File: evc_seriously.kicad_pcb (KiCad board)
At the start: 2 copper layers, 58 parts, among them J1 Screw_Terminal_01x10, J2 Conn_ARM_JTAG_SWD_10, J3 J_IN, J4 J_OUT, SW1 SW_Push, U1 TCA9517, U2 MPM3510A, U3 MPM3510A, U4 STM32F303K8Tx, U5 MIC2981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

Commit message: More routing of the board
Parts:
- C1, C2: footprint Capacitor_SMD:CP_Elec_5x5.8 -> Capacitor_SMD:C_0805_2012Metric
- moved JP1 94.0 mm to (190.2, 111.5)
- moved C11 91.7 mm to (166.1, 102.9), turned to 180 degrees
- moved U6 90.7 mm to (189.2, 116.8), turned to 90 degrees
- moved C13 86.1 mm to (185.4, 119.1), turned to 90 degrees
- moved JP2 85.2 mm to (186.4, 111.5)
- moved C10 83.2 mm to (166.1, 119.6)
- moved C9 80.4 mm to (155.0, 102.9)
- moved R10 67.9 mm to (90.9, 166.3), turned to 270 degrees
- moved C5 62.6 mm to (185.4, 114.6), turned to 90 degrees
- moved R11 57.1 mm to (90.9, 163.1), turned to 270 degrees
- moved C7 56.2 mm to (155.2, 110.5), turned to 180 degrees
- moved R3 56.2 mm to (91.7, 149.6), turned to 180 degrees
- moved U1 54.0 mm to (160.6, 104.8)
- moved C1 49.6 mm to (95.6, 160.5), turned to 180 degrees
- moved C3 48.7 mm to (168.9, 110.5), turned to 90 degrees
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
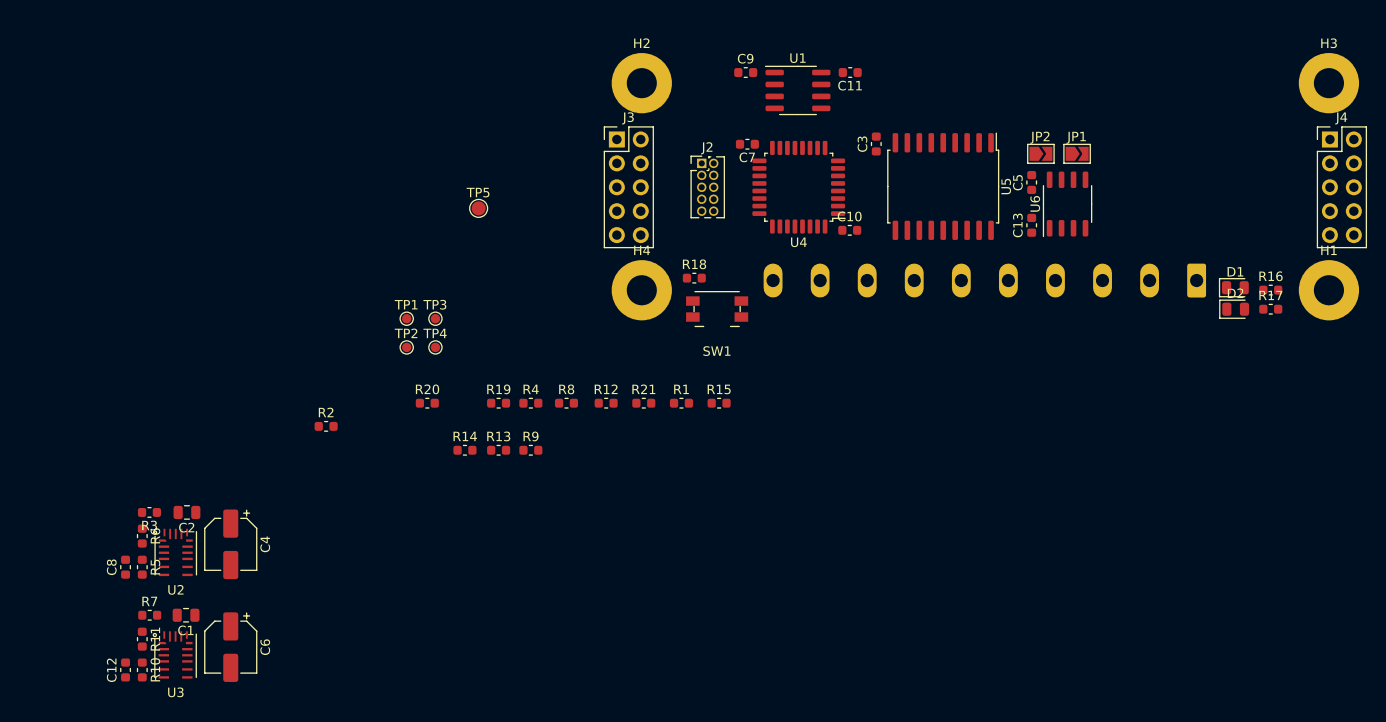
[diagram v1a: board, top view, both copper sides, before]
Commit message: Start routing nets
- Routed GND, +5V, and some +3V3
- TODO: swap positions of 3V3 and 5V bucks to simplify power bus
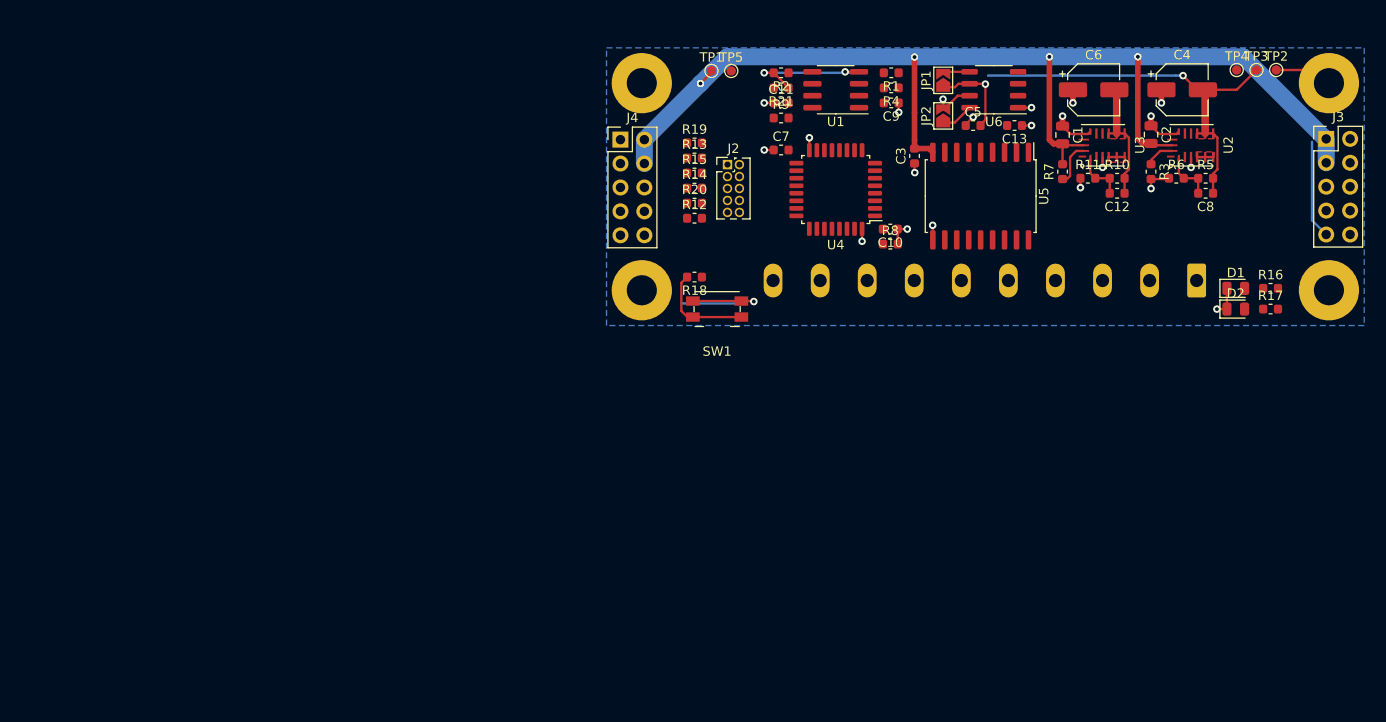
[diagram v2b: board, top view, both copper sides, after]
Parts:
- TP5: footprint TestPoint:TestPoint_Pad_D1.5mm -> TestPoint:TestPoint_Pad_D1.0mm
- moved C8 121.4 mm to (203.9, 115.7), turned to 180 degrees
- moved R5 120.3 mm to (203.9, 114.1), turned to 0 degrees
- moved C12 116.9 mm to (194.5, 115.7), turned to 180 degrees
- moved U2 116.6 mm to (202.6, 110.6), turned to 90 degrees
- moved R6 116.2 mm to (200.8, 114.1), turned to 0 degrees
- moved R10 116.0 mm to (194.5, 114.1), turned to 0 degrees
- moved U3 112.7 mm to (193.2, 110.6), turned to 90 degrees
- moved R3 112.4 mm to (198.1, 113.4), turned to 270 degrees
- moved C4 112.0 mm to (201.4, 104.7), turned to 0 degrees
- moved R11 111.8 mm to (191.4, 114.1), turned to 0 degrees
- moved C2 110.0 mm to (198.1, 109.5), turned to 270 degrees
- moved C6 109.1 mm to (192.0, 104.7), turned to 0 degrees
- moved R7 107.8 mm to (188.7, 113.4), turned to 90 degrees
- moved C1 106.2 mm to (188.7, 109.5), turned to 270 degrees
- moved TP2 97.0 mm to (211.4, 102.6)
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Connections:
- H1 pad 1: Net-(H1-Pad1) -> GND
- H2 pad 1: Net-(H2-Pad1) -> GND
- H3 pad 1: Net-(H3-Pad1) -> GND
- H4 pad 1: Net-(H4-Pad1) -> GND
- J3 pad 1: GND -> +24V
- J3 pad 10: +24V -> GND
- J3 pad 3: GND -> +24V
- J3 pad 5: GND -> /SDA_A
- J3 pad 6: +3V3 -> GND
- J3 pad 8: /SDA_A -> GND
- J3 pad 9: +24V -> +3V3
- J4 pad 10: +24V -> +3V3_B
- J4 pad 2: GND -> +24V
- J4 pad 4: GND -> +24V
- J4 pad 6: +3V3_B -> /SDA_B
- J4 pad 7: /SCL_B -> GND
- J4 pad 8: /SDA_B -> /SCL_B
- J4 pad 9: +24V -> GND
- U4 pad 20: /USR_SW -> Net-(U4-Pad20)
- U4 pad 25: Net-(U4-Pad25) -> /USR_SW
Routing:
- net +24V: track 0.00 -> 125.9 mm, vias 0 -> 4
- net GND: track 0.00 -> 73.9 mm, vias 0 -> 24
- net +5V: track 0.00 -> 52.6 mm, vias 0 -> 2
- net +3V3: track 0.00 -> 23.7 mm
- net /USR_SW: track 0.00 -> 10.5 mm
- net Net-(C8-Pad2): track 0.00 -> 5.38 mm
- net Net-(C12-Pad2): track 0.00 -> 5.38 mm
- net Net-(R7-Pad1): track 0.00 -> 4.67 mm
- net /VFIL-: track 0.00 -> 3.47 mm
- net /5V_EN: track 0.00 -> 3.09 mm
- net /VFIL+: track 0.00 -> 2.88 mm
- net Net-(U3-Pad4): track 0.00 -> 1.70 mm
- net Net-(U2-Pad4): track 0.00 -> 1.70 mm
- added copper zone on F.Cu, net +3V3
- added copper zone on F.Cu, net +5V
- added copper zone on B.Cu, net GND
- added copper zone on F.Cu, net Net-(U2-Pad4)
- added copper zone on F.Cu, net Net-(U3-Pad4)

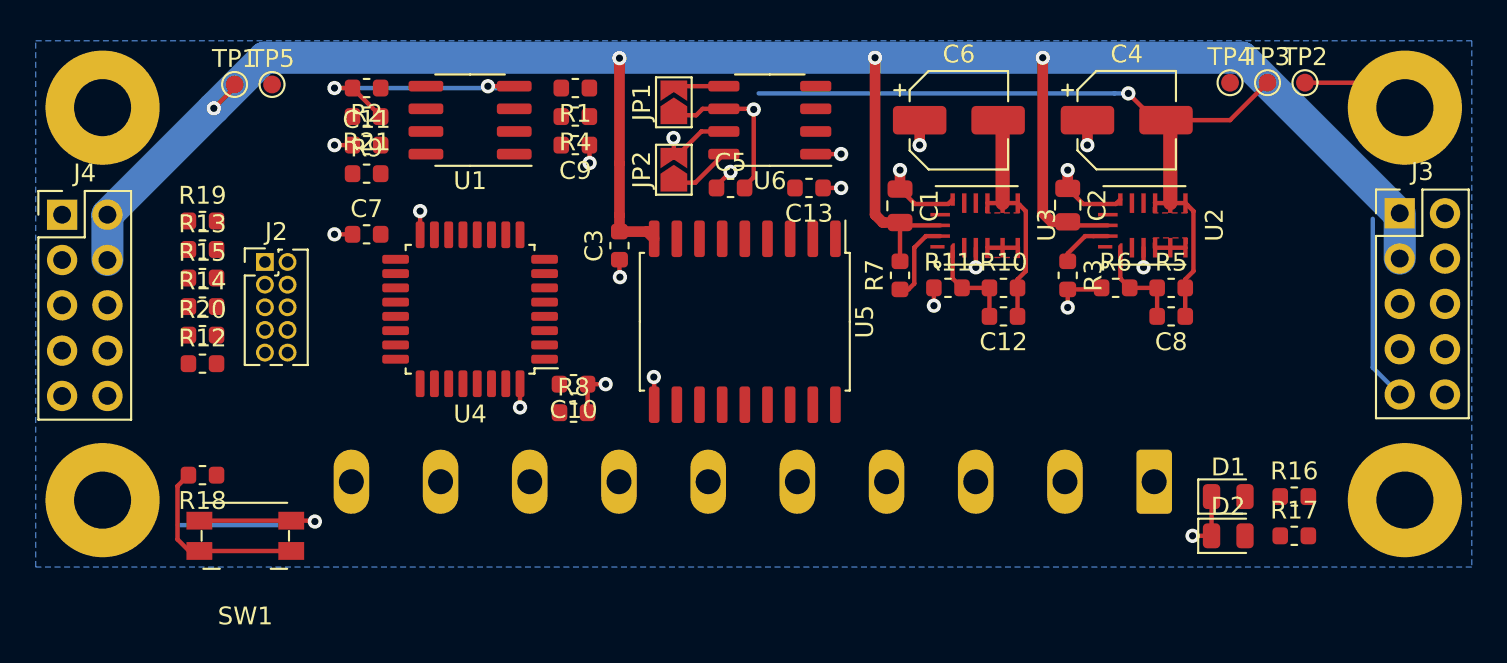
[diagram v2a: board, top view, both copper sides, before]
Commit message: More routing
- Swapped position of 3V3 and 5V buck converters
- Finish routing power nets
- Start routing data/enable lines
- Swap a bunch of microcontroller pins to reduce hopping
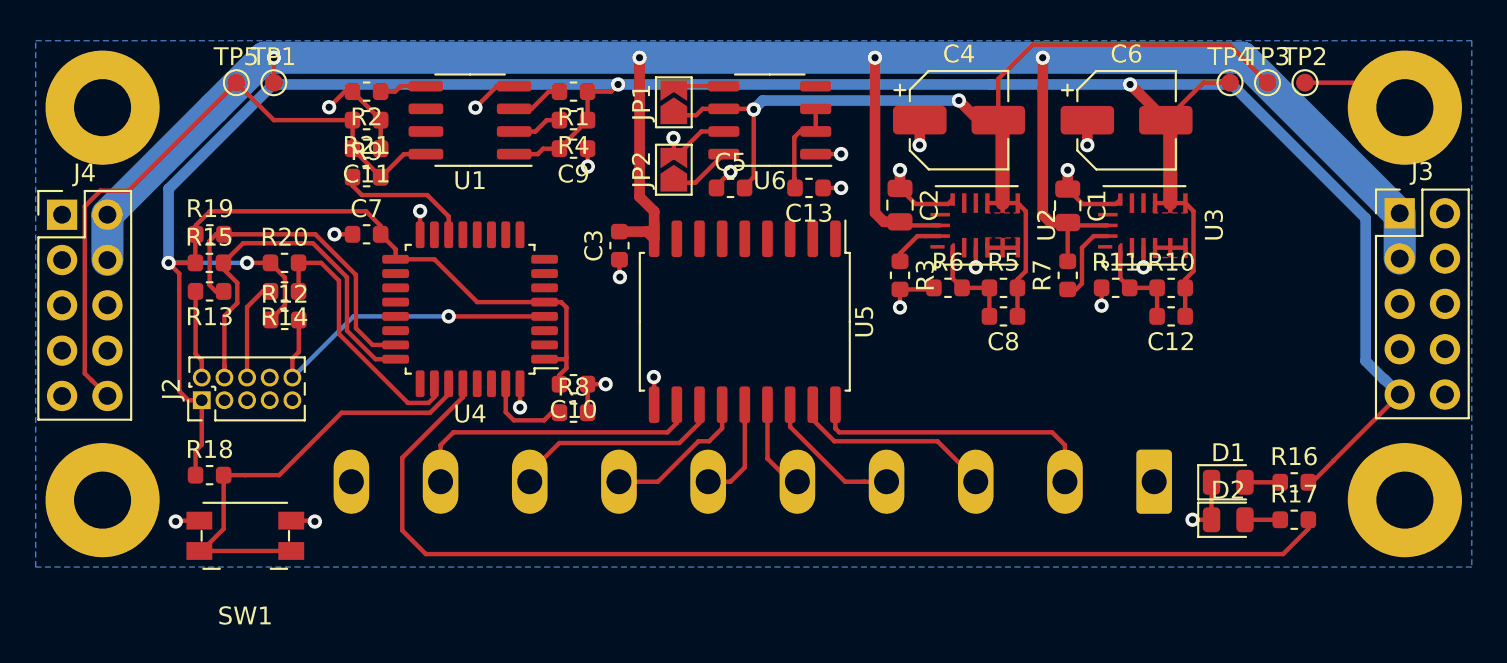
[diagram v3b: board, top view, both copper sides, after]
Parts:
- moved C1 9.40 mm to (198.1, 109.5)
- moved C12 9.40 mm to (203.9, 115.7)
- moved C2 9.40 mm to (188.7, 109.5)
- moved C6 9.40 mm to (201.4, 104.7)
- moved C8 9.40 mm to (194.5, 115.7)
- moved R10 9.40 mm to (203.9, 114.1)
- moved R11 9.40 mm to (200.8, 114.1)
- moved R3 9.40 mm to (188.7, 113.4)
- moved R5 9.40 mm to (194.5, 114.1)
- moved R6 9.40 mm to (191.4, 114.1)
- moved R7 9.40 mm to (198.1, 113.4)
- moved U2 9.40 mm to (193.2, 110.6)
- moved U3 9.40 mm to (202.6, 110.6)
- moved C4 9.40 mm to (192.0, 104.7)
- moved J2 8.52 mm to (149.6, 120.4), turned to 90 degrees
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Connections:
- JP1 pad 2: /VFIL+ -> /VFIL-
- JP2 pad 1: /VFIL- -> /VFIL+
- R9 pad 1: Net-(R9-Pad1) -> /SENSE
- U4 pad 14: Net-(U4-Pad14) -> /SENSE
- U4 pad 21: /USR_LED -> /I2C_EN
- U4 pad 22: Net-(U4-Pad22) -> /5V_EN
- U4 pad 25: /USR_SW -> Net-(U4-Pad25)
- U4 pad 27: /5V_EN -> /USR_SW
- U4 pad 28: /I2C_EN -> /USR_LED
- U4 pad 3: Net-(R9-Pad1) -> Net-(U4-Pad3)
- U6 pad 5: /VFIL+ -> /VFIL-
- U6 pad 8: /VFIL- -> /VFIL+
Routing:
- net +3V3: track 23.7 -> 180.4 mm, vias 0 -> 4
- net /USR_LED: track 0.00 -> 62.1 mm
- net +3V3_B: track 0.00 -> 37.6 mm
- net /SWDCLK: track 0.00 -> 22.3 mm
- net /SWDIO: track 0.00 -> 19.1 mm
- net /NRST: track 0.00 -> 18.9 mm, vias 0 -> 1
- net GND: track 73.9 -> 56.3 mm
- net /GRID: track 0.00 -> 16.8 mm
- net /SEG_A: track 0.00 -> 16.6 mm
- net /USR_SW: track 10.5 -> 25.7 mm
- net /SWO: track 0.00 -> 15.1 mm
- net /SEG_G: track 0.00 -> 12.2 mm
- net /SEG_B: track 0.00 -> 11.5 mm
- net /SEG_F: track 0.00 -> 8.35 mm
- net /SEG_C: track 0.00 -> 7.92 mm
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
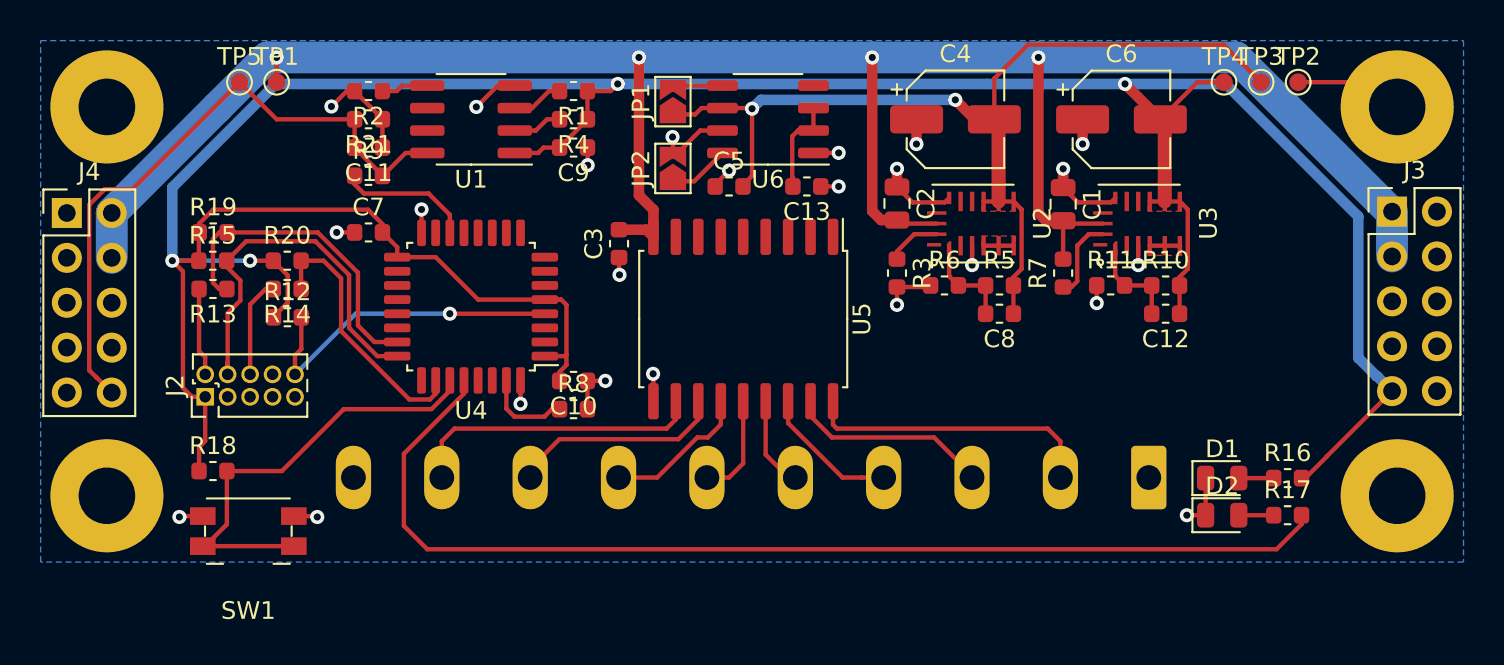
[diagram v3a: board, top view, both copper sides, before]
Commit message: Finish board routing, tidy silkscreen
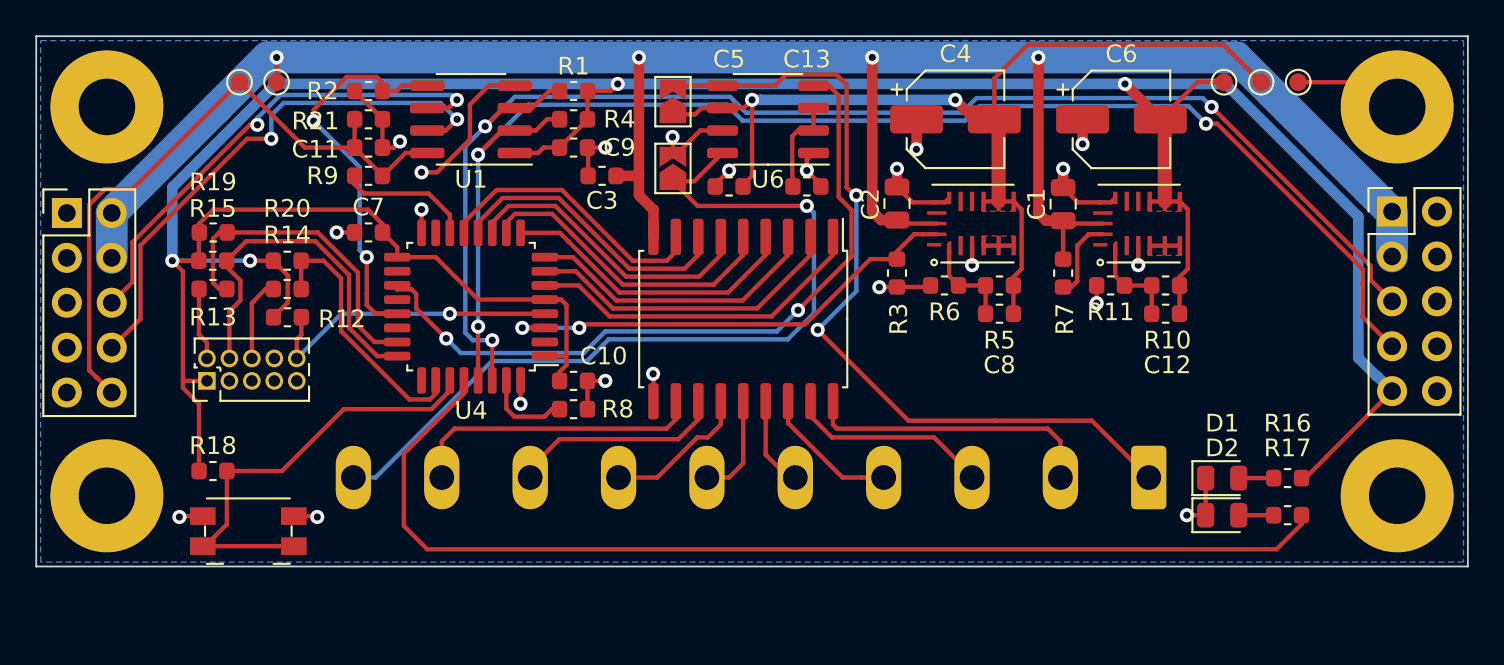
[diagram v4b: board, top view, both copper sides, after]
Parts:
- moved C3 3.95 mm to (172.0, 107.9), turned to 0 degrees
- moved J2 0.91 mm to (149.7, 119.5)
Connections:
- JP1 pad 2: /VFIL- -> /VFIL+
- JP2 pad 1: /VFIL+ -> /VFIL-
- U4 pad 22: /5V_EN -> Net-(U4-Pad22)
- U4 pad 3: Net-(U4-Pad3) -> /5V_EN
- U6 pad 5: /VFIL- -> /VFIL+
- U6 pad 8: /VFIL+ -> /VFIL-
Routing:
- net /SCL_A: track 2.80 -> 79.0 mm, vias 0 -> 3
- net /SDA_A: track 2.94 -> 79.1 mm, vias 0 -> 3
- net /VFIL-: track 2.88 -> 47.8 mm, vias 0 -> 1
- net /VFIL+: track 3.47 -> 47.7 mm, vias 0 -> 2
- net /FIL_PWM: track 0.00 -> 41.2 mm, vias 0 -> 2
- net /SCL_B: track 0.00 -> 32.6 mm, vias 0 -> 2
- net /SDA_B: track 0.00 -> 27.9 mm, vias 0 -> 2
- net /5V_EN: track 3.09 -> 27.2 mm, vias 0 -> 2
- net Net-(U4-Pad6): track 0.00 -> 20.3 mm
- net /I2C_EN: track 2.66 -> 22.7 mm, vias 0 -> 2
- net Net-(U4-Pad7): track 0.00 -> 18.9 mm
- net Net-(U4-Pad10): track 0.00 -> 17.6 mm
- net Net-(U4-Pad8): track 0.00 -> 17.5 mm
- net Net-(U4-Pad9): track 0.00 -> 17.2 mm
- net Net-(U4-Pad11): track 0.00 -> 17.1 mm
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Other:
- board outline added: 81 x 30 mm

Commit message: Fix regulator fill zones (but not really)
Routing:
- net Net-(U2-Pad4): track 1.70 -> 5.69 mm
- net +3V3: track 181.0 -> 185.0 mm
- net +5V: track 57.1 -> 60.9 mm
- net Net-(U3-Pad4): track 1.70 -> 5.15 mm
- removed copper zone on F.Cu, net +3V3
- removed copper zone on F.Cu, net +5V
- removed copper zone on F.Cu, net Net-(U2-Pad4)
- removed copper zone on F.Cu, net Net-(U3-Pad4)

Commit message: Fix silkscreen, add bling
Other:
- board text added: "2020"
- board text added: "EVC"
- board text added: "H"
- board text added: "SRSLY"
- board text added: "v1.1"
